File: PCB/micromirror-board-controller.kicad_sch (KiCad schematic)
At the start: 23 parts, among them J1 Barrel_Jack, J2 Conn_01x04_Female, J3 Conn_01x03_Female, J4 Conn_2Rows-51Pins, J6 USB_C_Receptacle_USB2.0, SW1 SW_Push, SW2 SW_Push, U1 Pico, U2 LM1117IMPX-5.0

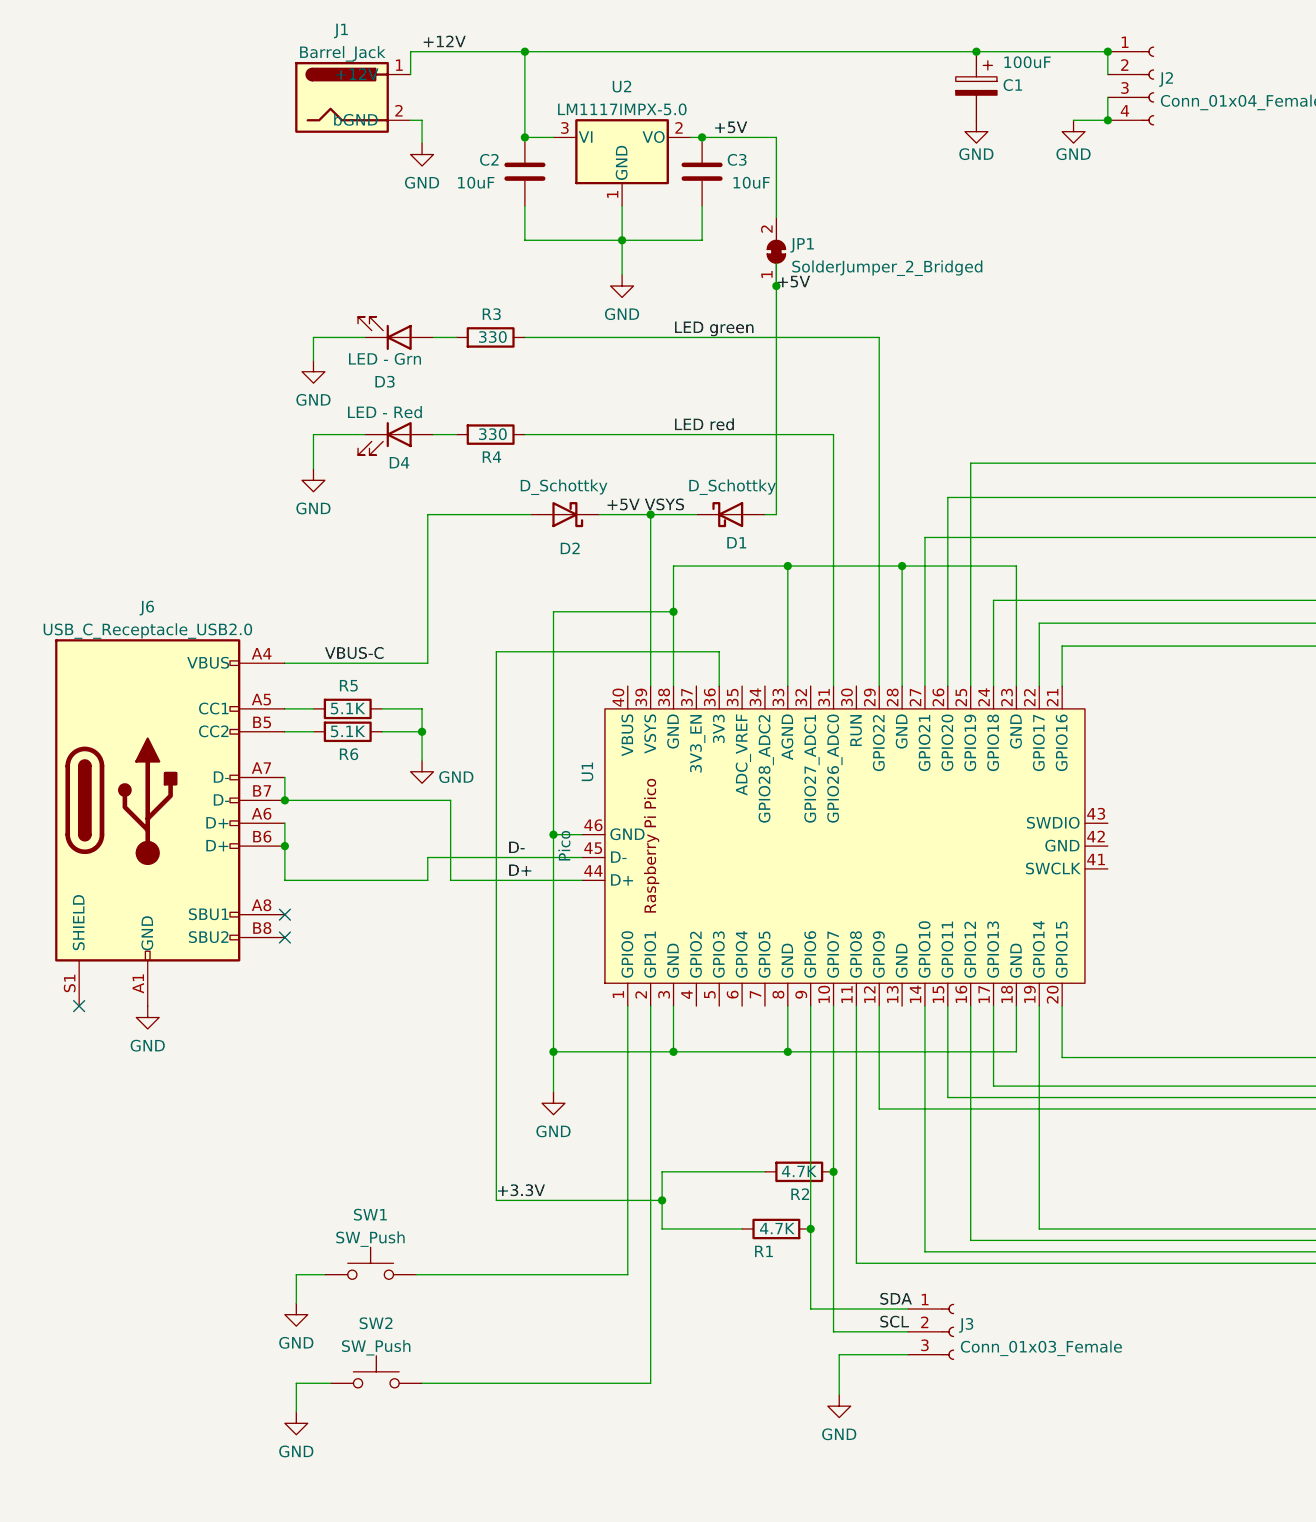
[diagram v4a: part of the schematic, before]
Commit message: Complete schematic parts list
Fix some parts without purchase link and clean up directory a bit.
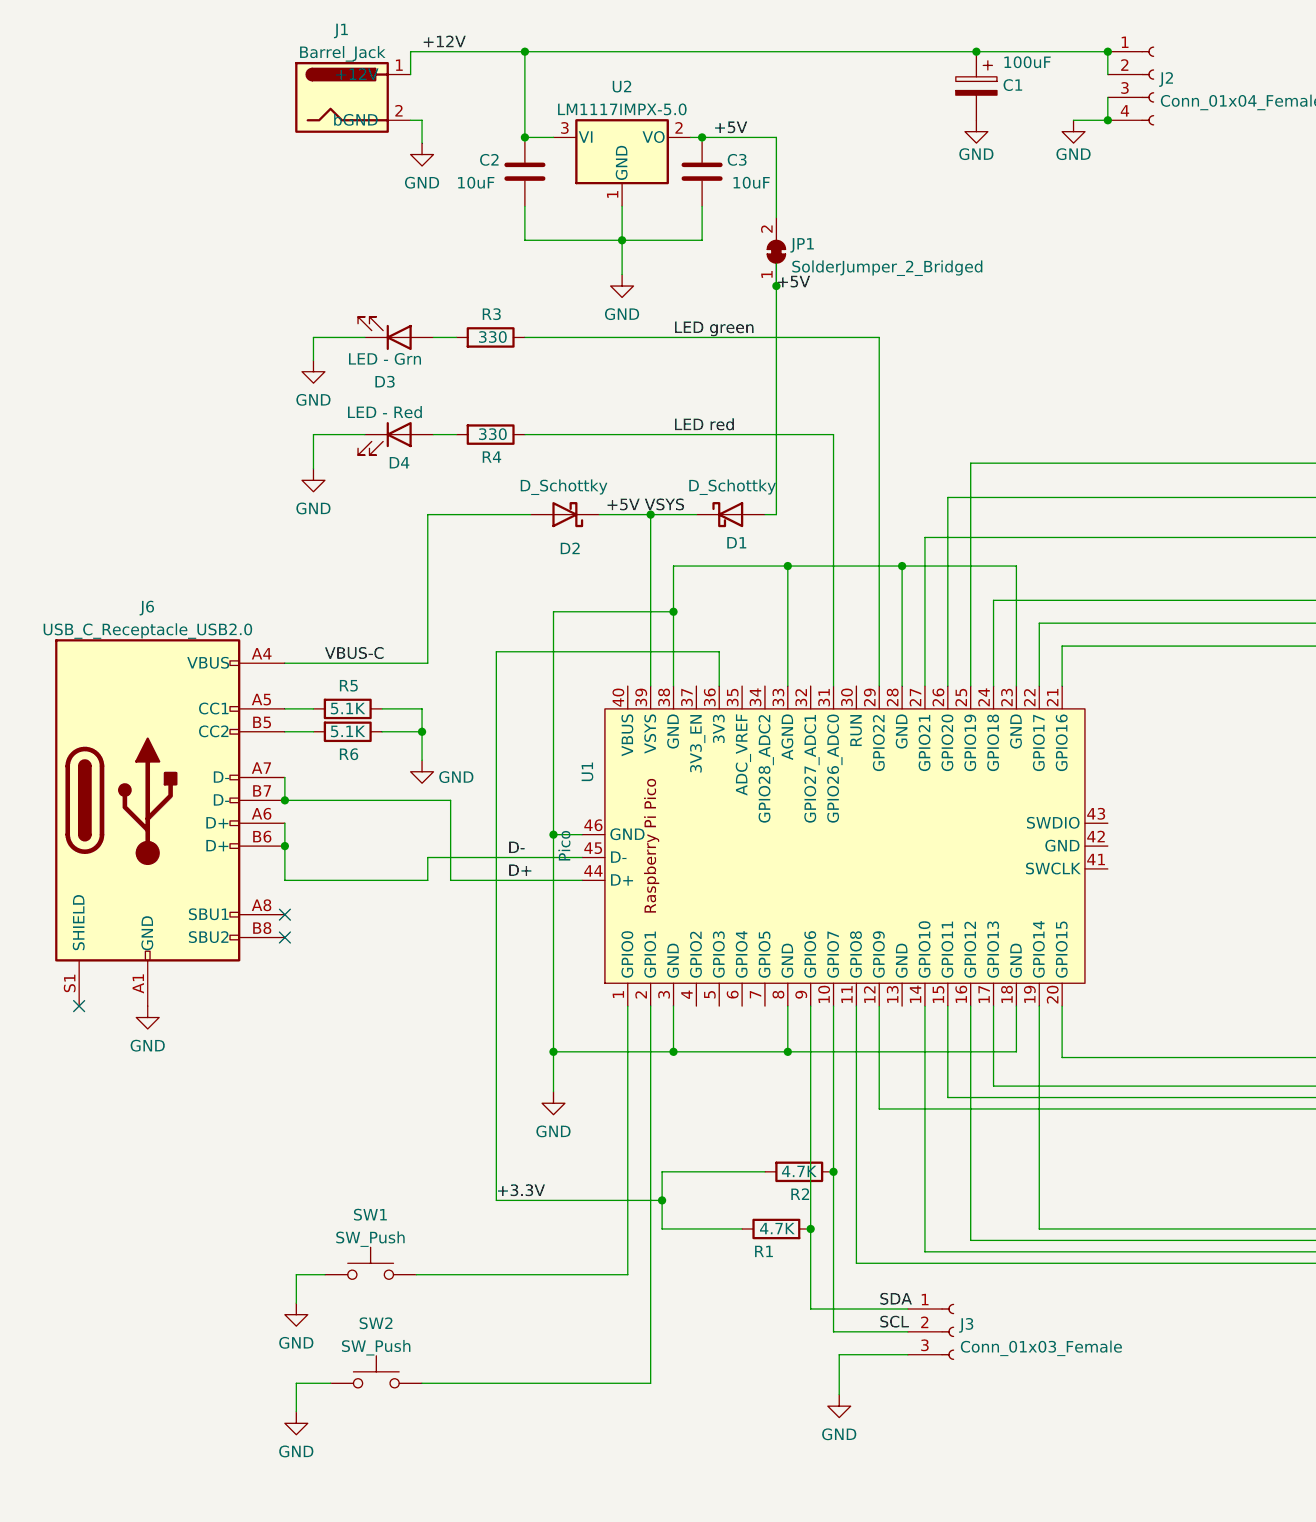
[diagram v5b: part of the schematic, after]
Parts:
- C1: Mouser (none) -> https://nl.mouser.com/ProductDetail/Lelon/VZL101M1ETR-0607?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; Mouser  https://nl.mouser.com/ProductDetail/Lelon/VZL101M1ETR-0607?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 -> (none)
- J1: Mouser (none) -> https://nl.mouser.com/ProductDetail/CUI-Devices/PJ-002B?qs=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
- J3: Mouser (none) -> https://nl.mouser.com/ProductDetail/Adafruit/4389?qs=xZ%2FP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; Mouser  https://nl.mouser.com/ProductDetail/Adafruit/4389?qs=xZ%2FP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 -> (none)
- J4: Mouser (none) -> https://nl.mouser.com/ProductDetail/Hirose-Connector/FH35C-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
- J6: Mouser (none) -> https://nl.mouser.com/ProductDetail/640-USB4105-GF-A-120
- U1: Mouser (none) -> https://nl.mouser.com/ProductDetail/Raspberry-Pi/SC0918?qs=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

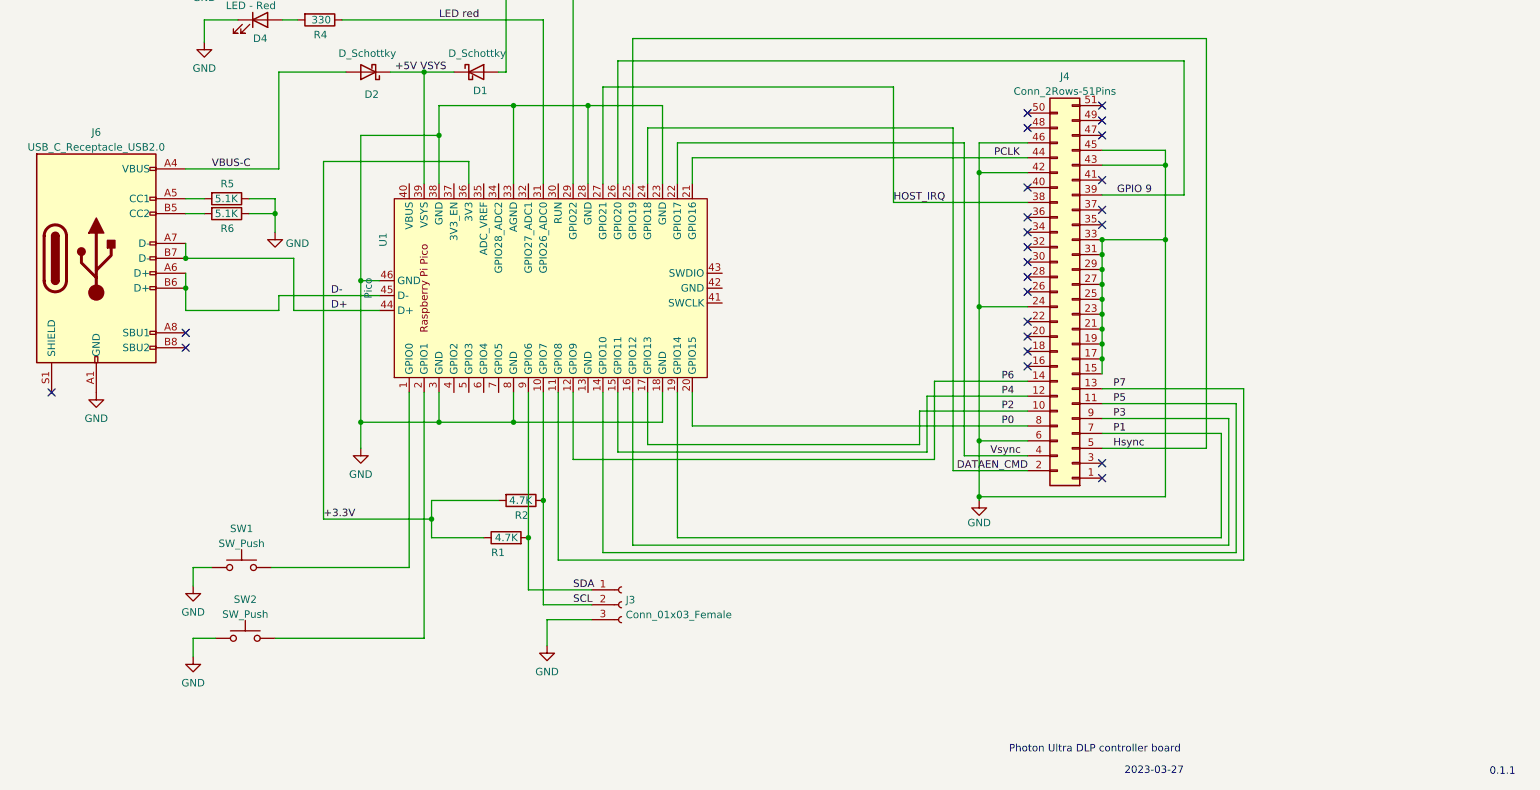
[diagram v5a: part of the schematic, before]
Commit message: Improved USB lines connectivity
Fixed the tricky blind SMD pad approach with cutout and backside wire connection. Added some 3D models for all board components. Reworked some silkscreen. Added a TX/RX serial connector for convenience
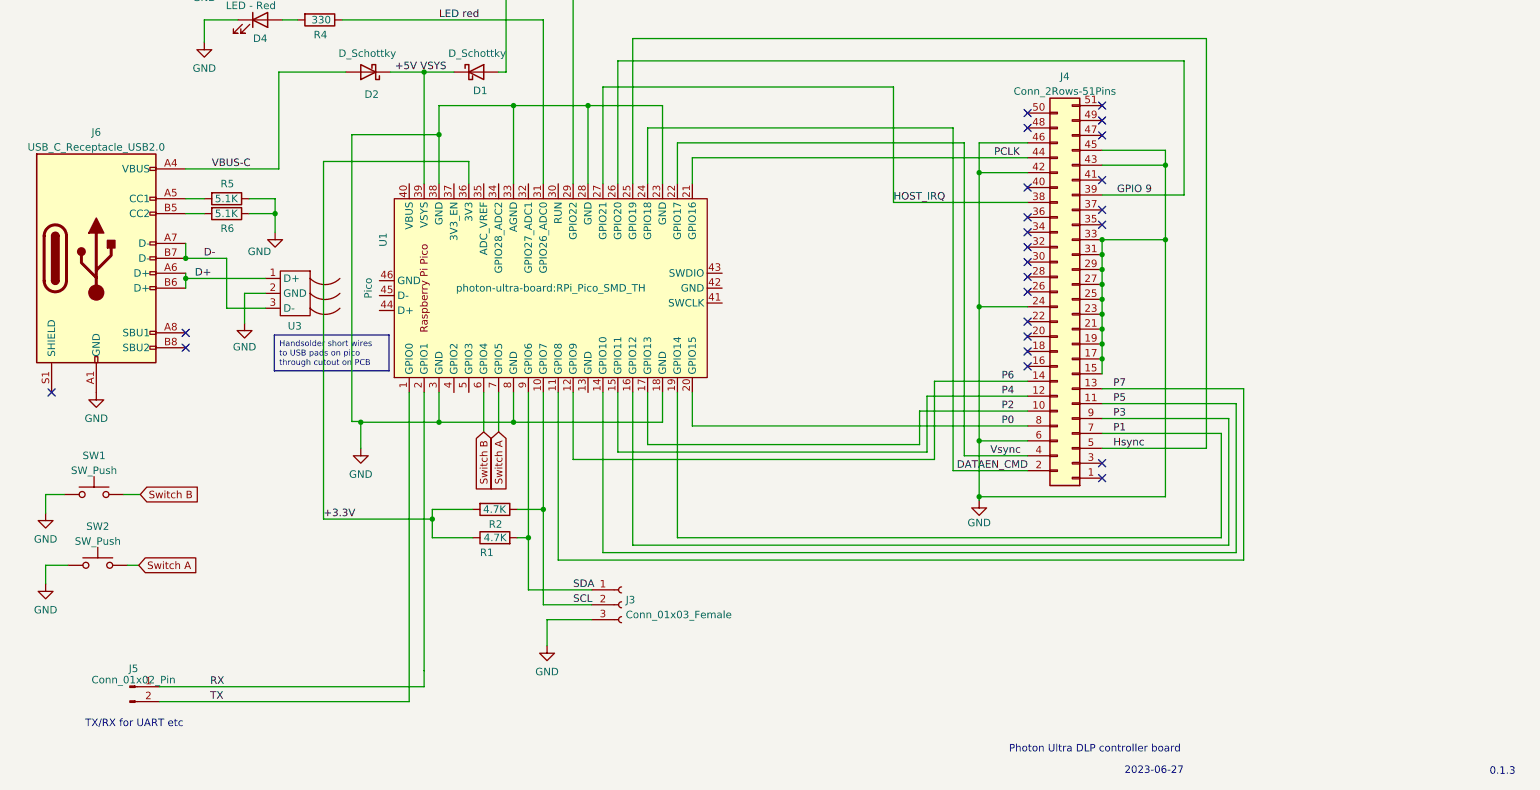
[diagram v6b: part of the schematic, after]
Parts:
- added J5: Conn_01x02_Pin, Connector_PinHeader_2.54mm:PinHeader_1x02_P2.54mm_Horizontal, symbol Connector:Conn_01x02_Pin
- added U3: ~, photon-ultra-board:usb-handsolder-pads, symbol photon-ultra-board:usb-handsolder-pads
- U1: footprint MCU_RaspberryPi_and_Boards:RPi_Pico_SMD_for-photon-ultra -> photon-ultra-board:RPi_Pico_SMD_TH
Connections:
- net D+: now also J6.A6 (D+), J6.B6 (D+), U3.1 (D+); no longer J6.A7 (D-), J6.B7 (D-), U1.44 (D+)
- net D-: now also J6.A7 (D-), J6.B7 (D-), U3.3 (D-); no longer J6.A6 (D+), J6.B6 (D+), U1.45 (D-)
- net GND: now also U3.2 (GND); no longer U1.46 (GND)
- net Switch B: now reaches SW1.2
- net Switch B: now also U1.6 (GPIO4); no longer U1.1 (GPIO0)
- net RX: now reaches U1.2 (GPIO1)
- net RX: now also J5.1 (Pin_1); no longer SW2.2
- net Switch A: now reaches U1.7 (GPIO5)
- net Switch A: now also SW2.2
- new net TX: J5.2 (Pin_2), U1.1 (GPIO0)
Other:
- note added: "0.1.3"
- note added: "2023-06-27"
- note added: "TX/RX for UART etc"
- note removed: "0.1.1"
- note removed: "2023-03-27"
- moved on the sheet: R1, R2, SW1, SW2
